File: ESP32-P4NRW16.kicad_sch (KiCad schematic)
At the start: 31 parts, among them J7 P4_DEBUG_PINS, U1 ESP32-P4NRW16, U11 W25Q256JWPIQ, U15 SN74LVC1G07DBVR, Y2 ECS-400-10-33B-CKM-TR

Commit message: SMA Update
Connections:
- net ESP_3V3: now also J7.11 (Pin_11)
- net GND: no longer J7.11 (Pin_11)
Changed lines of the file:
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@@
 	)
 	(junction
-		(at 25.4 182.88)
-		(diameter 0)
-		(color 0 0 0 0)
-	)
-	(junction
 		(at 25.4 177.8)
 		(diameter 0)
@@
 	(wire
 		(pts
-			(xy 25.4 180.34) (xy 25.4 182.88)
+			(xy 25.4 180.34) (xy 25.4 185.42)
 		)
 		(stroke
@@
 	(wire
 		(pts
-			(xy 25.4 182.88) (xy 29.21 182.88)
-		)
-		(stroke
-			(width 0)
-			(type default)
-		)
-	)
-	(wire
-		(pts
 			(xy 48.26 35.56) (xy 48.26 36.83)
 		)
@@
 	(wire
 		(pts
+			(xy 29.21 182.88) (xy 21.59 182.88)
+		)
+		(stroke
+			(width 0)
+			(type default)
+		)
+	)
+	(wire
+		(pts
 			(xy 44.45 115.57) (xy 44.45 116.84)
 		)
@@
 	(wire
 		(pts
+			(xy 21.59 182.88) (xy 21.59 181.61)
+		)
+		(stroke
+			(width 0)
+			(type default)
+		)
+	)
+	(wire
+		(pts
 			(xy 97.79 134.62) (xy 134.62 134.62)
 		)
@@
 	(wire
 		(pts
-			(xy 25.4 182.88) (xy 25.4 185.42)
-		)
-		(stroke
-			(width 0)
-			(type default)
-		)
-	)
-	(wire
-		(pts
 			(xy 41.91 182.88) (xy 68.58 182.88)
 		)
@@
 					(unit 1)
 				)
+			)
+		)
+	)
+	(symbol
+		(lib_id "power:+3.3V")
+		(at 21.59 181.61 0)
+		(mirror y)
+		(unit 1)
+		(exclude_from_sim no)
+		(in_bom yes)
+		(on_board yes)
+		(dnp no)
+		(property "Reference" "#PWR045"
+			(at 21.59 185.42 0)
+			(effects
+				(font
+					(size 1.27 1.27)
+				)
+				(hide yes)
+			)
+		)
+		(property "Value" "ESP_3V3"
+			(at 19.05 177.546 90)
+			(effects
+				(font
+					(size 1.27 1.27)
+				)
+			)
+		)
+		(property "Footprint" ""
+			(at 21.59 181.61 0)
+			(effects
+				(font
+					(size 1.27 1.27)
+				)
+				(hide yes)
+			)
+		)
+		(property "Datasheet" ""
+			(at 21.59 181.61 0)
+			(effects
+				(font
+					(size 1.27 1.27)
+				)
+				(hide yes)
+			)
+		)
+		(property "Description" "Power symbol creates a global label with name \"+3.3V\""
+			(at 21.59 181.61 0)
+			(effects
+				(font
+					(size 1.27 1.27)
+				)
+				(hide yes)
+			)
+		)
+		(pin "1"
+		)
+		(instances
+			(project "ESP32P4C5_Board"
+				(path "/d4a17687-8854-438f-9913-a6ddcff1a679/05efe0cf-c24a-4029-900a-f931e619b6bb"
+					(reference "#PWR045")
+					(unit 1)
+				)

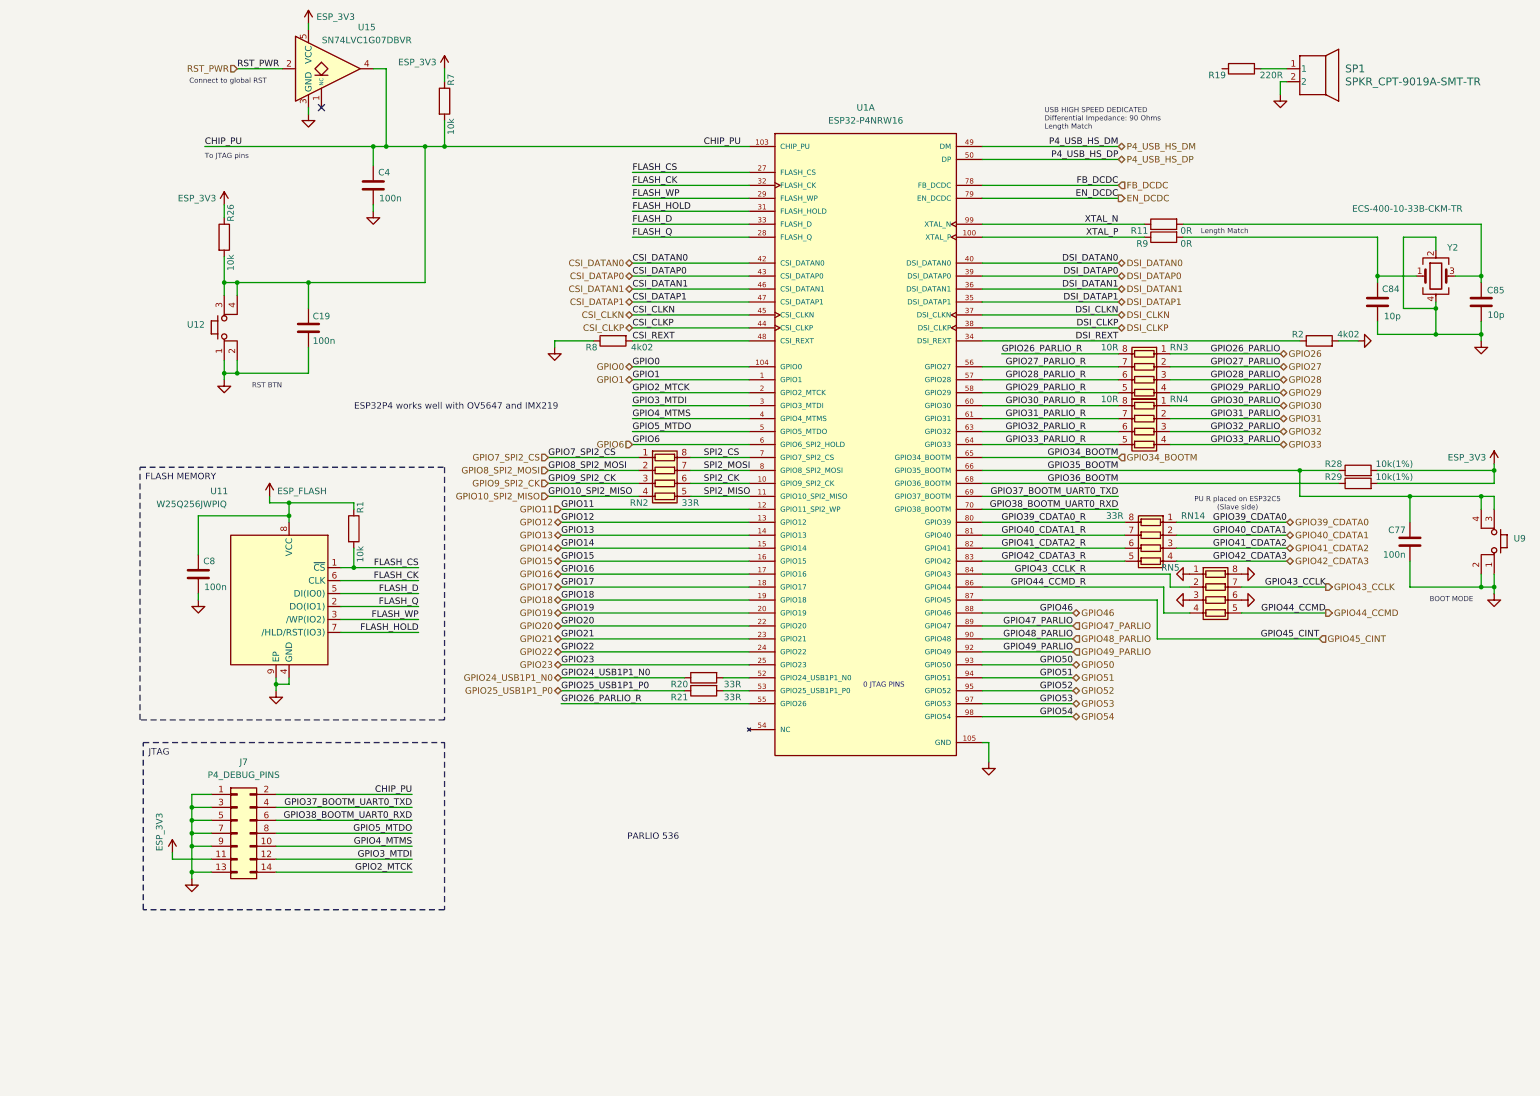
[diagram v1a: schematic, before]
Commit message: QSPI Memory Bus
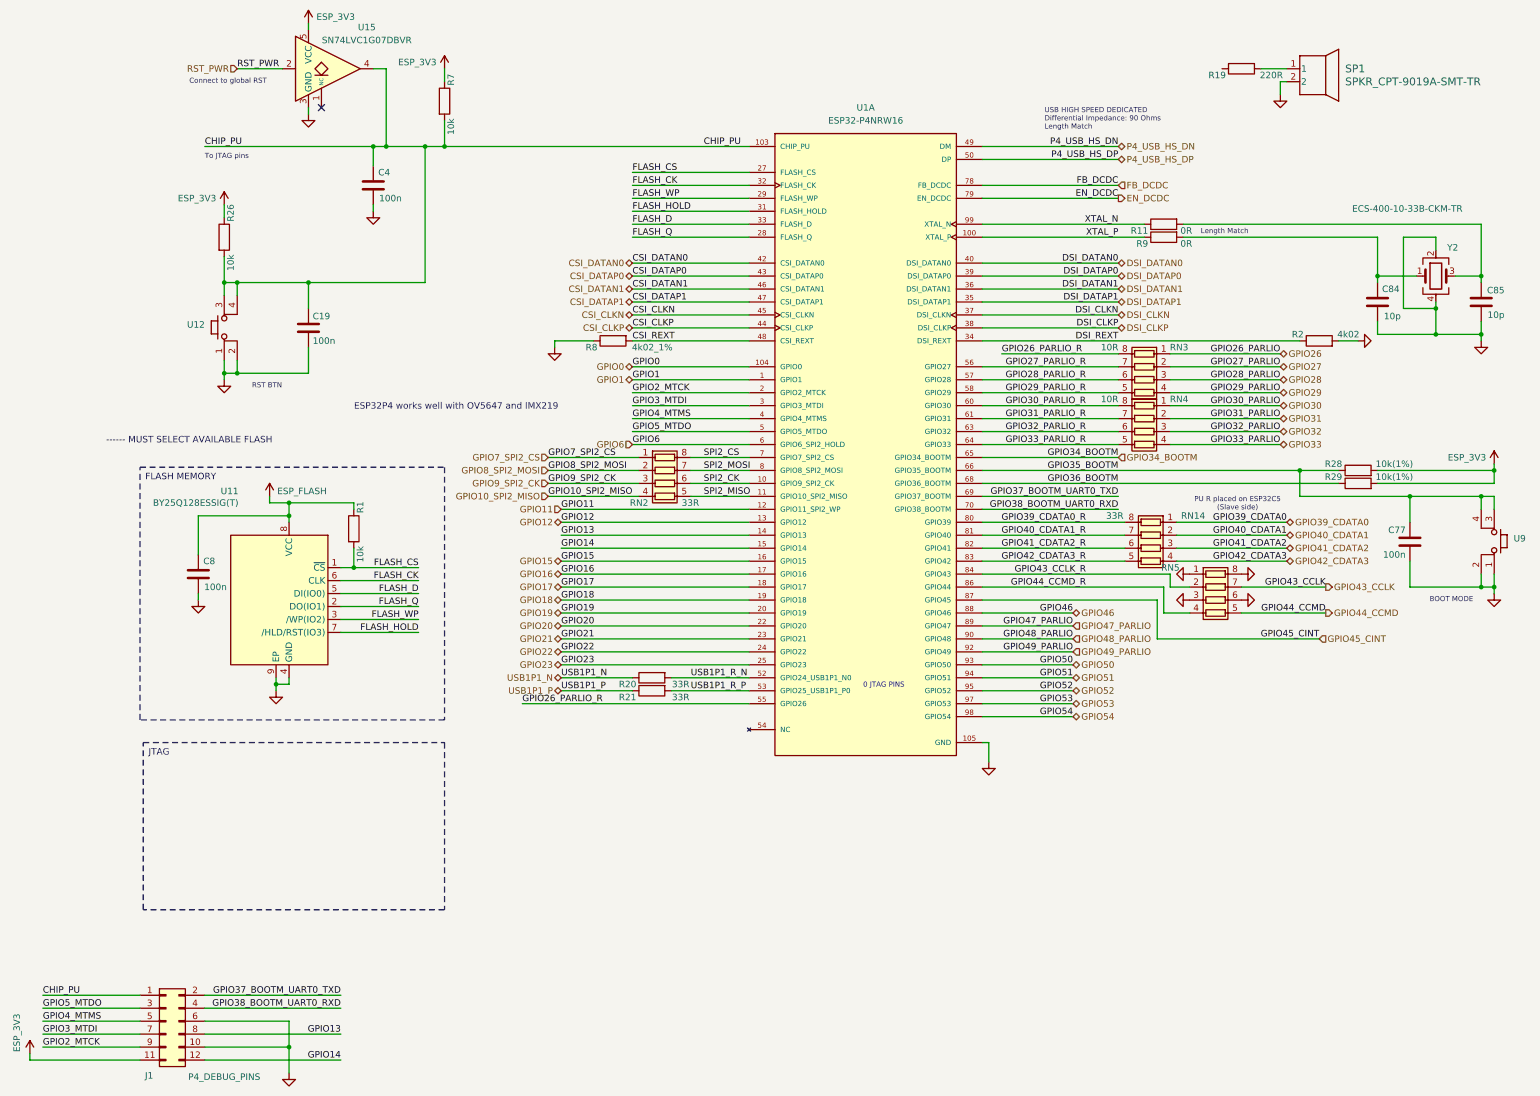
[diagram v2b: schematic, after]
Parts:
- removed J7: P4_DEBUG_PINS, Connector_PinHeader_2.54mm:PinHeader_2x07_P2.54mm_Horizontal, symbol Connector_Generic:Conn_02x07_Odd_Even
- added J1: P4_DEBUG_PINS, Connector_PinHeader_2.54mm:PinHeader_2x06_P2.54mm_Horizontal, symbol Connector_Generic:Conn_02x06_Odd_Even
- R8: value 4k02 -> 4k02_1%
- U11: value W25Q256JWPIQ -> BY25Q128ESSIG(T); footprint Package_SON:WSON-8-1EP_6x5mm_P1.27mm_EP3.4x4.3mm -> Package_SO:SOP-8_5.28x5.23mm_P1.27mm
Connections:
- net CHIP_PU: now also J1.1 (Pin_1)
- net ESP_3V3: now also J1.11 (Pin_11)
- net GND: now also J1.10 (Pin_10), J1.6 (Pin_6)
- net GPIO13: now also J1.8 (Pin_8)
- net GPIO14: now also J1.12 (Pin_12)
- net GPIO2_MTCK: now also J1.9 (Pin_9)
- net GPIO37_BOOTM_UART0_TXD: now also J1.2 (Pin_2)
- net GPIO38_BOOTM_UART0_RXD: now also J1.4 (Pin_4)
- net GPIO3_MTDI: now also J1.7 (Pin_7)
- net GPIO4_MTMS: now also J1.5 (Pin_5)
- net GPIO5_MTDO: now also J1.3 (Pin_3)
- net USB1P1_R_P: now reaches R21.2, U1.53 (GPIO25_USB1P1_P0)
- net USB1P1_R_N: now reaches R20.2, U1.52 (GPIO24_USB1P1_N0)
- net GPIO24_USB1P1_N0 renamed USB1P1_N
- net GPIO25_USB1P1_P0 renamed USB1P1_P
- net P4_USB_HS_DM renamed P4_USB_HS_DN
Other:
- note added: "------ MUST SELECT AVAILABLE FLASH"
- note removed: "PARLIO 536"
- moved on the sheet: R20, R21

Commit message: Interface Update
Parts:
- added C41: 100n, Capacitor_SMD:C_0603_1608Metric, symbol Device:C
- added R5: 10k, Resistor_SMD:R_0603_1608Metric, symbol Device:R
- added RN6: 33R, Resistor_SMD:R_Array_Convex_4x0402, symbol Device:R_Pack04
- added SW1: XUNPU DSHP-01-TS-GER, Button_Switch_SMD:SW_DIP_SPSTx01_Slide_Copal_CHS-01B_W7.62mm_P1.27mm, symbol Switch:SW_DIP_x01
- R28: footprint Resistor_SMD:R_0805_2012Metric_1 -> Resistor_SMD:R_0603_1608Metric
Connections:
- net CHIP_PU: no longer C19.2, R26.2, U12.3, U12.4
- net ESP_3V3: now also R5.1
- net GND: now also J1.12 (Pin_12), J1.2 (Pin_2), J1.4 (Pin_4), RN5.2 (R2.1), RN5.7 (R2.2), C41.1, RN6.4 (R4.1), RN6.5 (R4.2), SW1.2; no longer RN5.1 (R1.1), RN5.8 (R1.2)
- net GPIO14: no longer J1.12 (Pin_12)
- net GPIO16: now also R19.1
- net GPIO34_BOOTM: now also C41.2, R5.2, SW1.1
- net GPIO37_BOOTM_UART0_TXD: no longer J1.2 (Pin_2)
- net GPIO38_BOOTM_UART0_RXD: no longer J1.4 (Pin_4)
- net GPIO43_CCLK: now also RN5.8 (R1.2); no longer RN5.7 (R2.2)
- net GPIO43_CCLK_R: now also RN5.1 (R1.1); no longer RN5.2 (R2.1)
- net GPIO47_PARLIO: now also RN6.1 (R1.1); no longer U1.89 (GPIO47)
- net GPIO48_PARLIO: now also RN6.2 (R2.1); no longer U1.90 (GPIO48)
- net GPIO49_PARLIO: now also RN6.3 (R3.1); no longer U1.92 (GPIO49)
- net RST_PWR: now also C19.2, R26.2, U12.3, U12.4
- net SP+: now reaches R19.2, SP1.1
- net GPIO20 renamed GPIO20_SPI_MOSI
- net GPIO21 renamed GPIO21_SPI_MISO
- net GPIO22 renamed GPIO22_SPI_CLK
- net GPIO23 renamed GPIO23_SPI_CS
- new net GPIO47_PARLIO_R: RN6.8 (R1.2), U1.89 (GPIO47)
- new net GPIO48_PARLIO_R: RN6.7 (R2.2), U1.90 (GPIO48)
- new net GPIO49_PARLIO_R: RN6.6 (R3.2), U1.92 (GPIO49)
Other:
- note added: "Global Reset"
- note removed: "PU R placed on ESP32C5 (Slave side)"
- company: (none) -> Peter Hancak
- title: (none) -> ESP32P4C5_BOARD
- moved on the sheet: C19, C4, C77, J1, R19, R26, SP1, U12

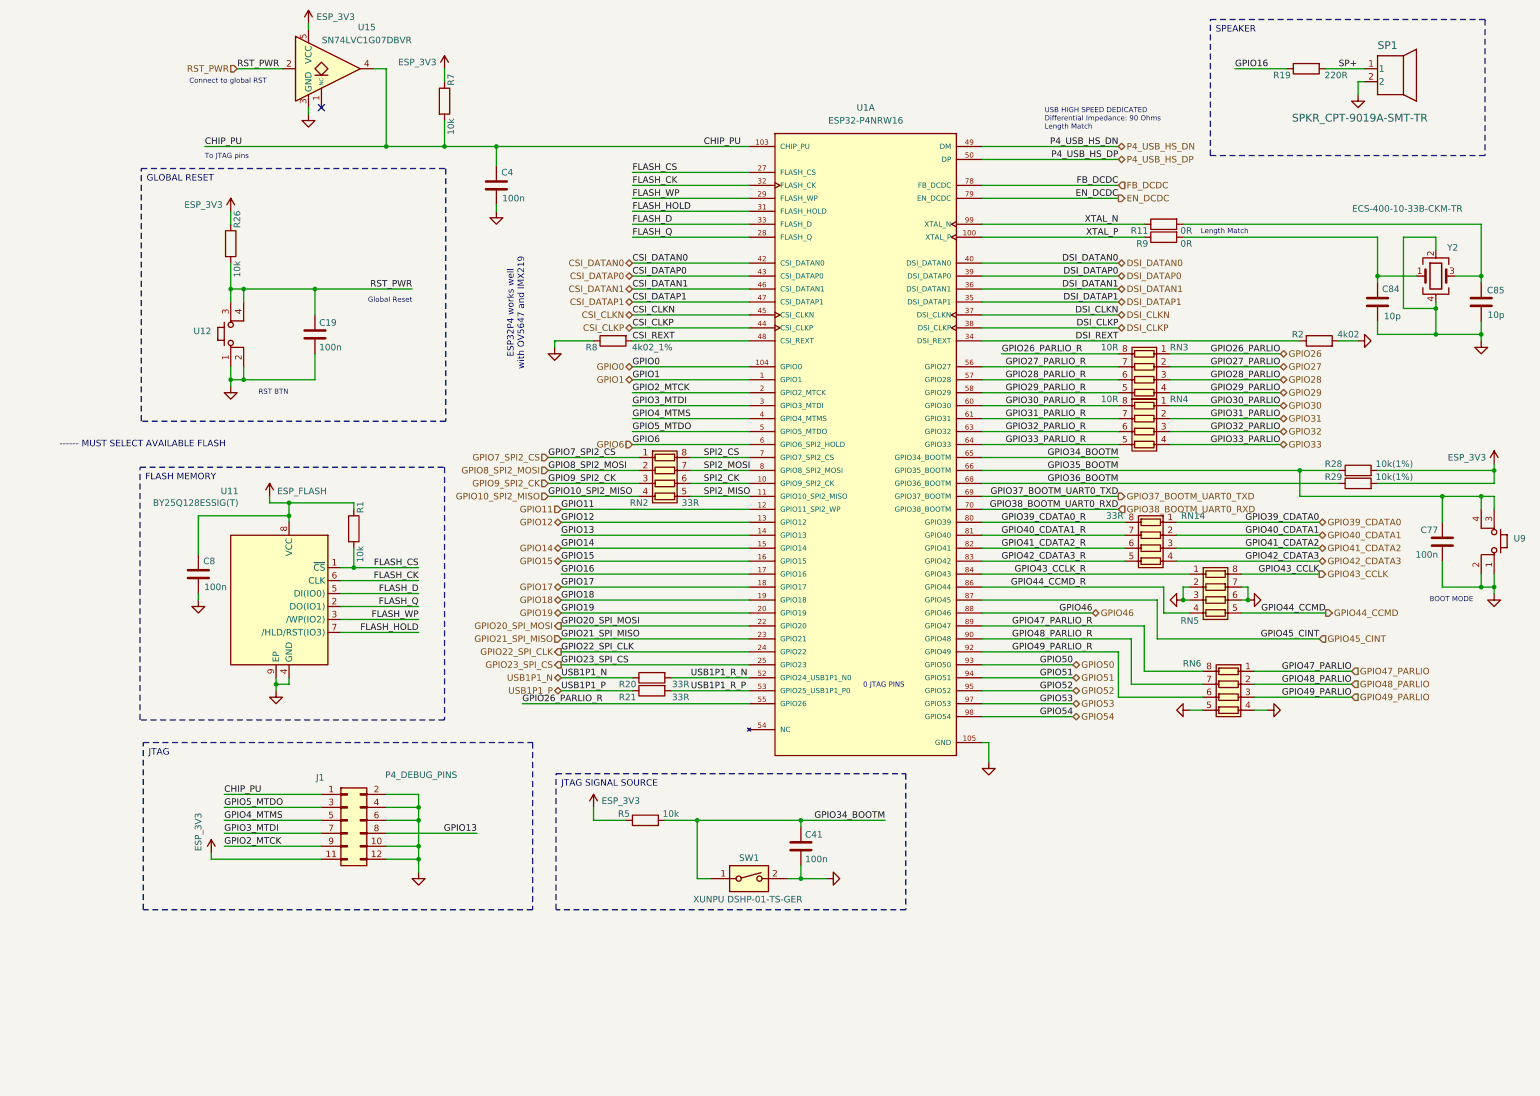
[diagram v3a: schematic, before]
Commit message: Small trace layout fixes
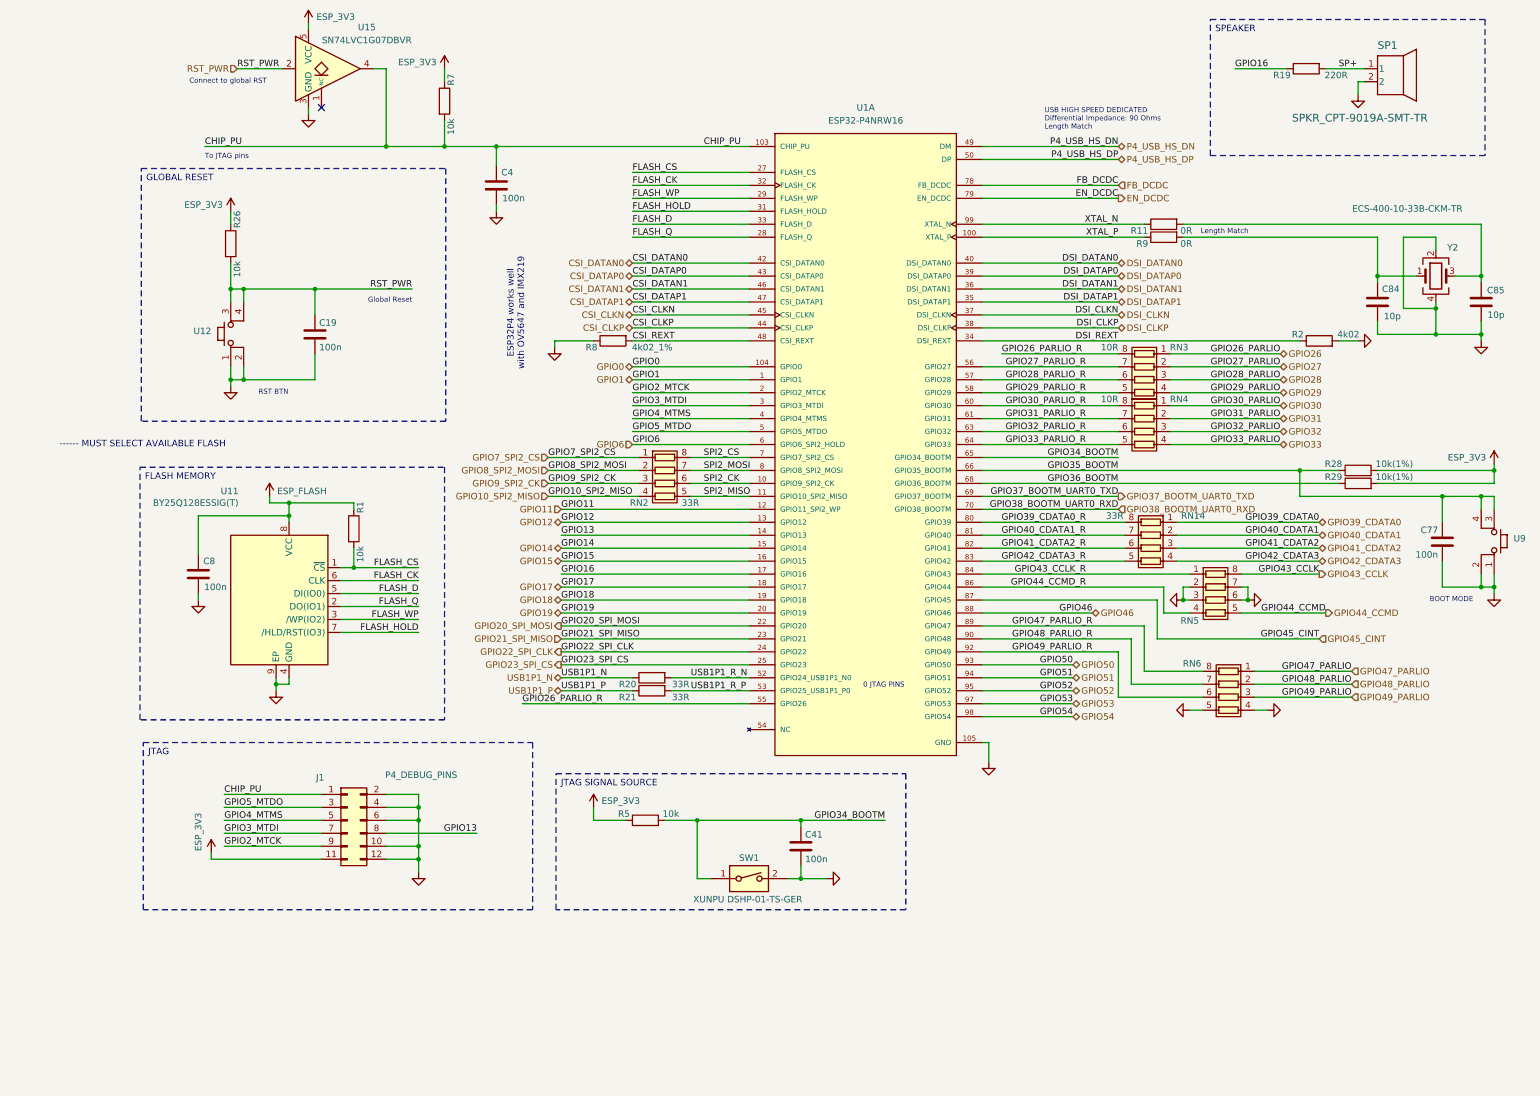
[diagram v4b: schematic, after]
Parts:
- U12, U9: value ~ -> (none)
